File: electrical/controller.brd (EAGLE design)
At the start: 101.6 x 25.4 mm, 27 parts, among them Q1 IRLIB9343PBF-ND, U1 MCP602P, U2 POLOLU_U1V11F5, U3 MCP4725, U4 MCP4725

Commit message: minor fixes on schematics.
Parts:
- U1: value MCP602P -> MCP6002
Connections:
- net 5V: now also R7.2
- net GND: no longer R7.2
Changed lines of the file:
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@@
 <element name="ST1" library="pie" package="2PIN_SCREW" value="2PIN_SCREW" x="-55.88" y="5.08"/>
 <element name="ST2" library="pie" package="2PIN_SCREW" value="2PIN_SCREW" x="-24.13" y="41.91"/>
-<element name="U1" library="linear" package="DIL08" value="MCP602P" x="-30.48" y="41.91"/>
+<element name="U1" library="linear" package="DIL08" value="MCP6002" x="-30.48" y="41.91"/>
 <element name="JP2" library="pie" package="1X02" value="" x="-26.67" y="58.42">
 <attribute name="PIE-INT-REF-NUM" value="BULK-STOCK" x="0" y="0" size="1.778" layer="27" display="off"/>
@@
 <contactref element="JP1" pad="2"/>
 <contactref element="JP1" pad="1"/>
-<contactref element="R7" pad="2"/>
 <contactref element="S3" pad="2"/>
 <contactref element="S3" pad="1"/>
@@
 <wire x1="-66.7512" y1="0.9906" x2="-70.4088" y2="0.9906" width="0" layer="19" extent="1-1"/>
 <wire x1="-60.2488" y1="0.9906" x2="-66.7512" y2="0.9906" width="0" layer="19" extent="1-1"/>
-<wire x1="-56.3" y1="-3.81" x2="-60.2488" y2="0.9906" width="0" layer="19" extent="1-1"/>
 <wire x1="-52.78" y1="8.38" x2="-60.2488" y2="0.9906" width="0" layer="19" extent="1-1"/>
-<wire x1="13.208" y1="5.588" x2="-52.78" y2="8.38" width="0" layer="19" extent="1-1"/>
-<wire x1="10.668" y1="5.588" x2="13.208" y2="5.588" width="0" layer="19" extent="1-1"/>
-<wire x1="-26.67" y1="38.1" x2="10.668" y2="5.588" width="0" layer="19" extent="1-1"/>
-<wire x1="-21.03" y1="45.21" x2="-26.67" y2="38.1" width="0" layer="19" extent="1-1"/>
-<wire x1="-23.23" y1="53.34" x2="-21.03" y2="45.21" width="0" layer="19" extent="1-1"/>
-<wire x1="-25.4" y1="58.42" x2="-23.23" y2="53.34" width="0" layer="19" extent="1-1"/>
-<wire x1="-16.88" y1="53.34" x2="-23.23" y2="53.34" width="0" layer="19" extent="1-1"/>
-<wire x1="-31.75" y1="58.42" x2="-25.4" y2="58.42" width="0" layer="19" extent="1-1"/>
-<wire x1="-34.29" y1="58.42" x2="-31.75" y2="58.42" width="0" layer="19" extent="1-1"/>
-<wire x1="-38.1" y1="59.7201" x2="-34.29" y2="58.42" width="0" layer="19" extent="1-1"/>
-<wire x1="-41.91" y1="59.7201" x2="-38.1" y2="59.7201" width="0" layer="19" extent="1-1"/>
+<wire x1="-50.8" y1="41.91" x2="-52.78" y2="8.38" width="0" layer="19" extent="1-1"/>
+<wire x1="-51.22" y1="53.34" x2="-50.8" y2="41.91" width="0" layer="19" extent="1-1"/>
+<wire x1="-41.91" y1="59.7201" x2="-51.22" y2="53.34" width="0" layer="19" extent="1-1"/>
+<wire x1="-38.1" y1="59.7201" x2="-41.91" y2="59.7201" width="0" layer="19" extent="1-1"/>
+<wire x1="-34.29" y1="58.42" x2="-38.1" y2="59.7201" width="0" layer="19" extent="1-1"/>
+<wire x1="-31.75" y1="58.42" x2="-34.29" y2="58.42" width="0" layer="19" extent="1-1"/>
 <wire x1="-35.98" y1="53.34" x2="-34.29" y2="58.42" width="0" layer="19" extent="1-1"/>
 <wire x1="-29.63" y1="53.34" x2="-31.75" y2="58.42" width="0" layer="19" extent="1-1"/>
-<wire x1="-51.22" y1="53.34" x2="-41.91" y2="59.7201" width="0" layer="19" extent="1-1"/>
-<wire x1="-50.8" y1="41.91" x2="-51.22" y2="53.34" width="0" layer="19" extent="1-1"/>
-<wire x1="8.128" y1="20.828" x2="-26.67" y2="38.1" width="0" layer="19" extent="1-1"/>
+<wire x1="-25.4" y1="58.42" x2="-31.75" y2="58.42" width="0" layer="19" extent="1-1"/>
+<wire x1="-23.23" y1="53.34" x2="-25.4" y2="58.42" width="0" layer="19" extent="1-1"/>
+<wire x1="-16.88" y1="53.34" x2="-23.23" y2="53.34" width="0" layer="19" extent="1-1"/>
+<wire x1="-21.03" y1="45.21" x2="-23.23" y2="53.34" width="0" layer="19" extent="1-1"/>
+<wire x1="-26.67" y1="38.1" x2="-21.03" y2="45.21" width="0" layer="19" extent="1-1"/>
+<wire x1="8.128" y1="20.828" x2="-21.03" y2="45.21" width="0" layer="19" extent="1-1"/>
+<wire x1="10.668" y1="5.588" x2="8.128" y2="20.828" width="0" layer="19" extent="1-1"/>
+<wire x1="13.208" y1="5.588" x2="10.668" y2="5.588" width="0" layer="19" extent="1-1"/>
 </signal>
 <signal name="5V">
@@
 <contactref element="Q1" pad="2"/>
 <contactref element="C1" pad="1"/>
-<wire x1="-53.34" y1="41.91" x2="-104.14" y2="1.27" width="0" layer="19" extent="1-1"/>
+<contactref element="R7" pad="2"/>
+<wire x1="-56.3" y1="-3.81" x2="-104.14" y2="1.27" width="0" layer="19" extent="1-1"/>
+<wire x1="-38.1" y1="2.54" x2="-56.3" y2="-3.81" width="0" layer="19" extent="1-1"/>
+<wire x1="-53.34" y1="41.91" x2="-38.1" y2="2.54" width="0" layer="19" extent="1-1"/>
 <wire x1="-41.06" y1="53.34" x2="-53.34" y2="41.91" width="0" layer="19" extent="1-1"/>
 <wire x1="-37.68" y1="53.34" x2="-41.06" y2="53.34" width="0" layer="19" extent="1-1"/>
@@
 <wire x1="-20.74" y1="59.69" x2="-18.68" y2="53.34" width="0" layer="19" extent="1-1"/>
 <wire x1="-34.29" y1="45.72" x2="-31.33" y2="53.34" width="0" layer="19" extent="1-1"/>
-<wire x1="13.208" y1="20.828" x2="-34.29" y2="45.72" width="0" layer="19" extent="1-1"/>
-<wire x1="-38.1" y1="2.54" x2="13.208" y2="20.828" width="0" layer="19" extent="1-1"/>
+<wire x1="13.208" y1="20.828" x2="-18.68" y2="53.34" width="0" layer="19" extent="1-1"/>
 </signal>
 <signal name="COIL">

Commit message: Route Done
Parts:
- added U$12, U$8: (no value), pie:STAND-OFF-TIGHT
- moved C1 204.8 mm to (96.0, 20.1)
- moved JP3 194.6 mm to (78.0, 21.6), turned to 270 degrees
- moved S_PWR 175.4 mm to (65.3, 20.8)
- moved R7 134.4 mm to (76.5, 10.4), turned to 180 degrees
- moved U2 134.3 mm to (82.0, 14.7), turned to 180 degrees
- moved R4 126.7 mm to (61.7, 9.40)
- moved Q1 124.5 mm to (86.4, 5.84), turned to 270 degrees
- moved R3 121.0 mm to (61.7, 12.2)
- moved JP1 120.8 mm to (82.0, 21.6), turned to 90 degrees
- moved R2 119.4 mm to (61.7, 4.06)
- moved JP2 118.6 mm to (86.1, 21.6), turned to 90 degrees
- moved ST1 113.2 mm to (55.6, 24.4), turned to 180 degrees
- moved U4 101.1 mm to (46.7, 9.91)
- moved U3 100.6 mm to (46.7, 4.32)
- moved S2 100.0 mm to (5.08, 12.4)
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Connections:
- net N$1 renamed VBAT
- net 5V: no longer U4.6
- net COIL: no longer UC1.7
- net GND: now also U4.6
- net INT: now also UC1.7
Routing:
- net DRIVE: track 0.00 -> 47.3 mm
- net 5V: track 0.00 -> 39.3 mm, vias 0 -> 2
- net SCL: track 0.00 -> 34.2 mm, vias 0 -> 1
- net SDA: track 0.00 -> 32.4 mm
- net VBAT: track 0.00 -> 24.6 mm
- net COIL: track 0.00 -> 21.7 mm
- net RST: track 0.00 -> 19.6 mm
- net AUX: track 0.00 -> 18.9 mm
- net N$2: track 0.00 -> 18.4 mm
- net USR2: track 0.00 -> 16.7 mm
- net INT: track 0.00 -> 16.5 mm
- net V1: track 0.00 -> 14.9 mm
- net N$3: track 0.00 -> 14.2 mm
- net USR1: track 0.00 -> 12.8 mm
- net N$5: track 0.00 -> 6.90 mm
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- added copper zone on layer 16, net 5V
- added copper zone on layer 1, net GND
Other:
- board text added: "5V GND"
- board text added: "ALL RESISTORS 10k"
- board text added: "COIL"
- board text added: "Douglas Hutchings Double Pendulum Driver Rev A"
- board text added: "GND AUX"
- board text added: "GND GND"
- board text added: "ON OFF CHARGE"
- board text added: "RESET"
- board text added: "VBAT GND"

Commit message: Small board fixes
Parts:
- moved S2 0.36 mm to (4.83, 12.7)
- moved U$8 0.36 mm to (19.1, 12.7)
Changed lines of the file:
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@@
 <attribute name="NAME" x="3.175" y="8.89" size="1.27" layer="25" font="vector" ratio="10" rot="R180"/>
 </element>
-<element name="S2" library="pie" package="TACTILE-PTH" value="" x="5.08" y="12.446">
-<attribute name="PIE-INT-REF-NUM" value="pth_pushbutton" x="5.08" y="12.446" size="1.778" layer="27" display="off"/>
+<element name="S2" library="pie" package="TACTILE-PTH" value="" x="4.826" y="12.7">
+<attribute name="PIE-INT-REF-NUM" value="pth_pushbutton" x="4.826" y="12.7" size="1.778" layer="27" display="off"/>
 </element>
 <element name="C1" library="SparkFun-Capacitors" package="CPOL-RADIAL-1000UF-63V" value="10mF" x="96.012" y="20.066" smashed="yes">
@@
 <attribute name="VALUE" x="74.803" y="24.13" size="1.27" layer="27" font="vector" rot="R270"/>
 </element>
-<element name="U$8" library="pie" package="STAND-OFF-TIGHT" value="" x="19.304" y="12.446"/>
+<element name="U$8" library="pie" package="STAND-OFF-TIGHT" value="" x="19.05" y="12.7"/>
 <element name="U$12" library="pie" package="STAND-OFF-TIGHT" value="" x="70.358" y="12.7"/>
 </elements>
@@
 <wire x1="16.002" y1="5.334" x2="11.684" y2="9.652" width="0.254" layer="1"/>
 <wire x1="11.684" y1="9.652" x2="8.8646" y2="9.652" width="0.254" layer="1"/>
-<wire x1="8.8646" y1="9.652" x2="8.3312" y2="10.1854" width="0.254" layer="1"/>
-<wire x1="8.3312" y1="10.1854" x2="1.8288" y2="10.1854" width="0.254" layer="1"/>
+<wire x1="8.8646" y1="9.652" x2="8.0772" y2="10.4394" width="0.254" layer="1"/>
+<wire x1="8.0772" y1="10.4394" x2="1.5748" y2="10.4394" width="0.254" layer="1"/>
 </signal>
 <signal name="VBAT">

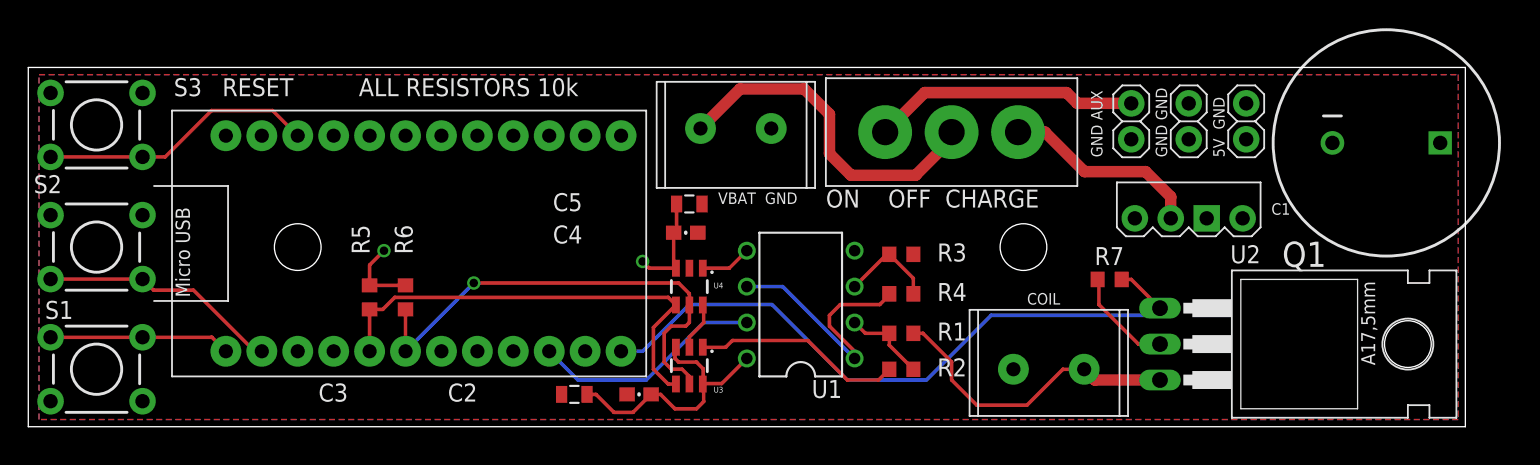
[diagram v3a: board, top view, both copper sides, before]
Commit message: Rev B PCB changes
New parts, re-route.
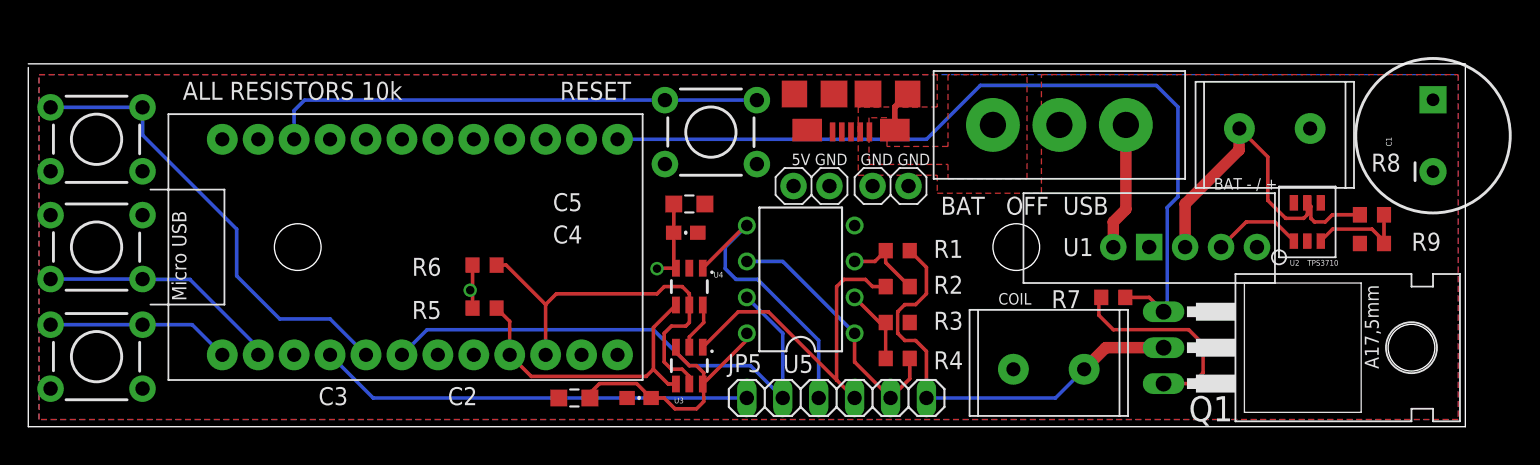
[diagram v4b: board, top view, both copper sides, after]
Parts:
- removed JP3: (no value), pie:1X02
- added JP5: (no value), pinhead:1X06
- added R8: 115k, pie:R0603
- added R9: 10K, pie:R0603
- added S4: (no value), pie:TACTILE-PTH
- added U5: MCP6002, linear:DIL08
- added USB1: USB-OTGMICRO-AB, pie:USB-MICRO-AB
- C1: value 10mF -> 1000uF; device SparkFun-Capacitors:CPOL-RADIAL-1000UF-63V -> SparkFun-Capacitors:CPOL-RADIAL-1000UF-25V
- U1: value MCP6002 -> POLOLU_D24V22F5; device linear:DIL08 -> custom_parts:POLOLU_D24V22F5
- U2: value POLOLU_U1V11F5 -> TPS3710; device custom_parts:POLOLU_U1V11F5 -> custom_parts:SOT6
- moved ST1 38.1 mm to (93.7, 24.4)
- moved JP2 31.1 mm to (55.4, 17.0), turned to 180 degrees
- moved U1 26.1 mm to (80.5, 11.4), turned to 0 degrees
- moved JP1 21.6 mm to (61.0, 17.0), turned to 180 degrees
- moved U2 8.39 mm to (90.4, 14.5), turned to 0 degrees
- moved R5 8.16 mm to (32.3, 8.38), turned to 180 degrees
- moved S_PWR 7.64 mm to (72.9, 21.3), turned to 180 degrees
- moved R6 6.04 mm to (32.3, 11.4), turned to 180 degrees
- moved R2 5.85 mm to (61.5, 9.91)
- moved R1 5.85 mm to (61.5, 12.4)
- moved R3 4.83 mm to (61.5, 7.37)
- moved R4 4.58 mm to (61.5, 4.83), turned to 180 degrees
- moved C1 3.34 mm to (99.3, 20.6), turned to 90 degrees
- moved R7 1.30 mm to (76.7, 9.14)
- moved S3 1.02 mm to (4.83, 20.3), turned to 180 degrees
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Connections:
- removed net AUX: JP3.1, S_PWR.P1
- new net N$1: U1.4, U2.P1
- new net N$6: R8.1, R9.2, U2.P3
- new net SHIFT: JP5.5, R4.1, U5.1, U5.6
- new net USR3: S3.3, S3.4, UC1.2
- net 5V: now also C1.+, Q1.3, S_PWR.P2, U5.8; no longer C1.1, Q1.2, U1.8, U2.1
- net COIL: now also JP5.6, Q1.2; no longer Q1.3
- net DRIVE: now also UC1.10; no longer UC1.9
- net GND: now also C1.-, JP5.1, R9.1, S4.1, S4.2, U1.2, U2.P2, U2.P4, U2.P6, U5.4, USB1.P$10, USB1.P$11, USB1.P$5, USB1.P$6, USB1.P$7, USB1.P$8, USB1.P$9; no longer C1.2, JP3.2, U1.4, U2.2
- net INT: now also JP5.2, U5.7, UC1.3; no longer U1.7, UC1.7
- net N$2: now also S_PWR.P3, USB1.P$1; no longer R4.1, U1.1, U1.6
- net N$3: now also S_PWR.P1, U1.1; no longer S_PWR.P3, U2.3
- net N$4: now also U5.3; no longer U1.2
- net N$5: now also U5.2; no longer U1.3
- net RST: now also S4.3, S4.4; no longer S3.3, S3.4
- net SCL: now also UC1.7; no longer UC1.3
- net SDA: now also UC1.6; no longer UC1.2
- net V1: now also JP5.4
- net V2: now also JP5.3, U5.5; no longer U1.5
- net VBAT: now also R8.2, U1.3, U2.P5; no longer S_PWR.P2
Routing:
- net GND: track 3.44 -> 37.1 mm
- net USR3: track 0.00 -> 32.6 mm
- net INT: track 16.5 -> 37.8 mm
- net AUX: track 18.9 -> 0.00 mm
- net SHIFT: track 0.00 -> 18.7 mm
- net N$2: track 18.4 -> 0.00 mm
- net V2: track 3.63 -> 20.8 mm
- net RST: track 19.6 -> 35.1 mm
- net DRIVE: track 47.3 -> 59.9 mm
- net SDA: track 32.4 -> 21.9 mm
- net COIL: track 21.7 -> 31.7 mm
- net V1: track 14.9 -> 24.8 mm
- net N$6: track 0.00 -> 7.20 mm
- net N$1: track 0.00 -> 6.45 mm
- net SCL: track 34.2 -> 28.0 mm, vias 1 -> 0
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- added copper zone on layer 1, net N$2
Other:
- board size 101.6 x 25.4 mm -> 101.6 x 25.7 mm
- board text added: "BAT + / -"
- board text added: "BAT - / +"
- board text added: "BAT OFF USB"
- board text added: "Douglas Hutchings Double Pendulum Driver Rev B"
- board text removed: "Douglas Hutchings Double Pendulum Driver Rev A"
- board text removed: "GND AUX"
- board text removed: "ON OFF CHARGE"
- board text removed: "VBAT GND"

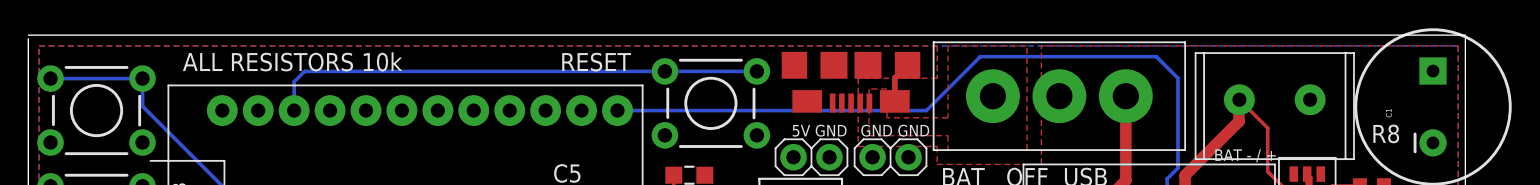
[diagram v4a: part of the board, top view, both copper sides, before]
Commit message: small border change.
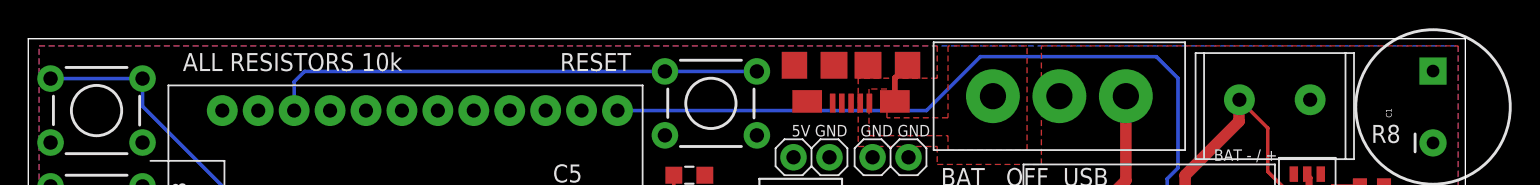
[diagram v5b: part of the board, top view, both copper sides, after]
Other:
- board size 101.6 x 25.7 mm -> 101.6 x 25.4 mm
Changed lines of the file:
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@@
 Double Pendulum Driver
 Rev B</text>
-<wire x1="0" y1="25.654" x2="101.6" y2="25.654" width="0" layer="20"/>
+<wire x1="0" y1="25.4" x2="101.6" y2="25.4" width="0" layer="20"/>
 <text x="83.82" y="16.764" size="0.8128" layer="25" font="vector">BAT - / +</text>
 <text x="85.09" y="18.796" size="0.8128" layer="26" font="vector" rot="MR180">BAT + / -</text>

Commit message: Rename JP5 to JP3
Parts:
- renumbered JP5 to JP3
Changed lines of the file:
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@@
 <element name="U$8" library="pie" package="STAND-OFF-TIGHT" value="" x="19.05" y="12.7"/>
 <element name="U$12" library="pie" package="STAND-OFF-TIGHT" value="" x="69.85" y="12.7"/>
-<element name="JP5" library="pinhead" package="1X06" value="" x="57.15" y="2.032"/>
+<element name="JP3" library="pinhead" package="1X06" value="" x="57.15" y="2.032"/>
 <element name="Q1" library="transistor-fet" package="TO220" value="IRLIB9343PBF-ND " x="86.614" y="5.588" smashed="yes" rot="R270">
 <attribute name="NAME" x="82.042" y="0.381" size="1.778" layer="25" ratio="10"/>
@@
 <wire x1="47.752" y1="7.366" x2="47.752" y2="8.5399" width="0.254" layer="1"/>
 <wire x1="47.752" y1="8.5399" x2="47.686" y2="8.6059" width="0.254" layer="1"/>
-<contactref element="JP5" pad="1"/>
+<contactref element="JP3" pad="1"/>
 <contactref element="USB1" pad="P$6"/>
 <contactref element="USB1" pad="P$7"/>
@@
 <contactref element="ST2" pad="P$2"/>
 <contactref element="R1" pad="1"/>
-<contactref element="JP5" pad="6"/>
+<contactref element="JP3" pad="6"/>
 <contactref element="Q1" pad="2"/>
 <wire x1="80.264" y1="5.588" x2="76.174" y2="5.588" width="0.8128" layer="1"/>
@@
 <contactref element="U5" pad="1"/>
 <contactref element="R4" pad="1"/>
-<contactref element="JP5" pad="5"/>
+<contactref element="JP3" pad="5"/>
 <wire x1="62.318" y1="4.826" x2="62.318" y2="3.39" width="0.254" layer="1"/>
 <wire x1="62.318" y1="3.39" x2="60.96" y2="2.032" width="0.254" layer="1"/>
@@
 <contactref element="U5" pad="5"/>
 <contactref element="U4" pad="1"/>
-<contactref element="JP5" pad="3"/>
+<contactref element="JP3" pad="3"/>
 <wire x1="50.8" y1="14.224" x2="50.7039" y2="14.224" width="0.254" layer="1"/>
 <wire x1="50.7039" y1="14.224" x2="47.686" y2="11.2061" width="0.254" layer="1"/>
@@
 <contactref element="R2" pad="1"/>
 <contactref element="U3" pad="1"/>
-<contactref element="JP5" pad="4"/>
+<contactref element="JP3" pad="4"/>
 <wire x1="60.618" y1="9.906" x2="59.69" y2="9.906" width="0.254" layer="1"/>
 <wire x1="59.69" y1="9.906" x2="59.182" y2="10.414" width="0.254" layer="1"/>
@@
 <signal name="INT">
 <contactref element="U5" pad="7"/>
-<contactref element="JP5" pad="2"/>
+<contactref element="JP3" pad="2"/>
 <contactref element="UC1" pad="3"/>
 <wire x1="53.34" y1="2.032" x2="53.34" y2="6.604" width="0.254" layer="16"/>

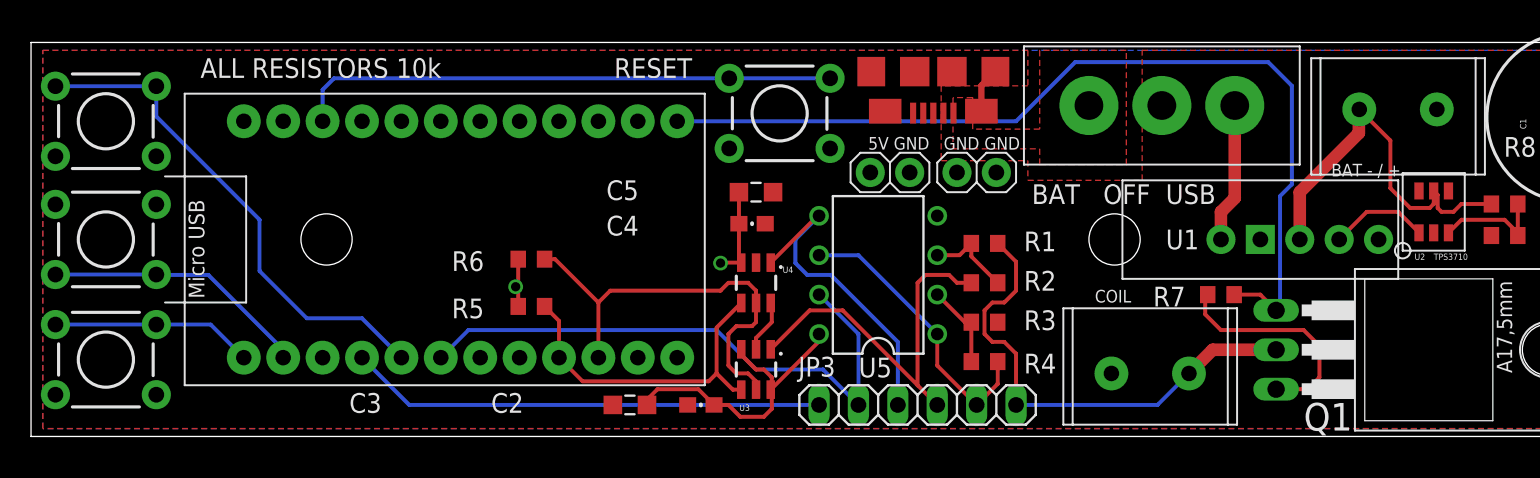
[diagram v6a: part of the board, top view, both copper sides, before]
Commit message: Fix Rev B erratta
Hole sizes for screw terminals
Pour clearance
Silkscreen Fixes
Revision Numbers
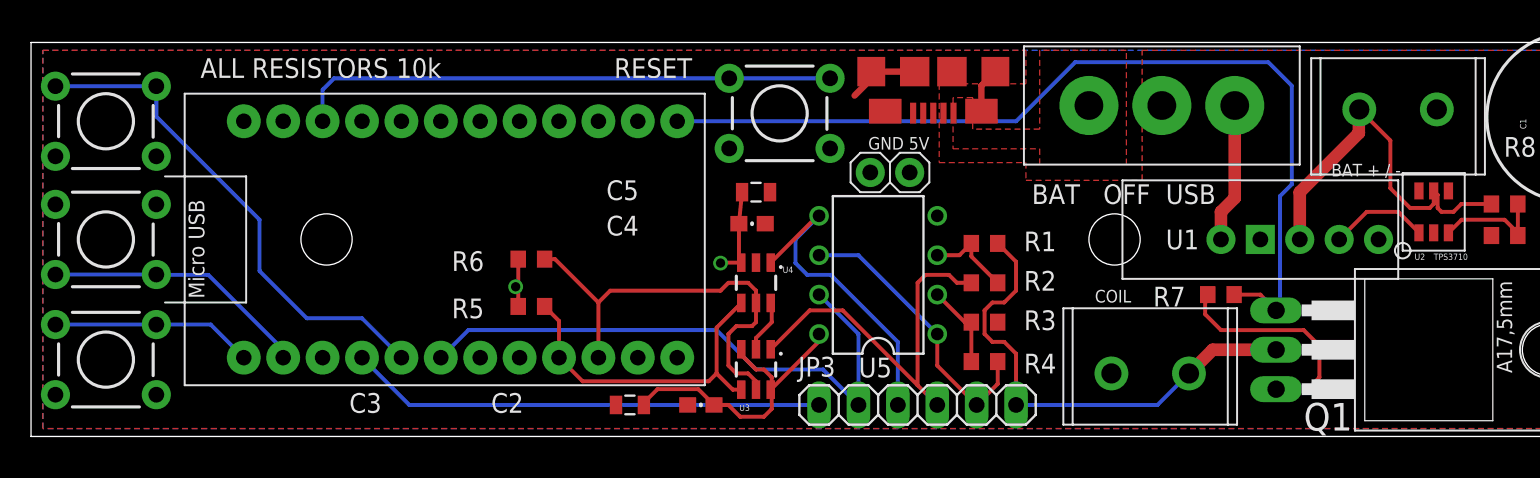
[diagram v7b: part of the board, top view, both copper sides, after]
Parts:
- removed JP1: (no value), pie:1X02
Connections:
- net GND: no longer JP1.1, JP1.2
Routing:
- net GND: track 37.1 -> 41.8 mm
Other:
- board text added: "Douglas Hutchings Double Pendulum Driver Rev C"
- board text added: "GND 5V"
- board text removed: "5V GND"
- board text removed: "Douglas Hutchings Double Pendulum Driver Rev B"
- board text removed: "GND GND"
